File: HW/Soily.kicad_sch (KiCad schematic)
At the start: 52 parts, among them J1 USB4105-GF-A, SW1 Reset, U1 ESP32-H2-MINI-1, U2 USBLC6-2SC6, U3 AP2112K-3.3, U4 SHT30-DIS, U5 625L3C040M00000, U6 FDC2212DNTR, Y1 ABS07-32.768KHZ-T

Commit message: Cleanup component selection
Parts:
- C1: Digikey Part Number (none) -> 490-10475-1-ND; Part Number (none) -> GRM188R61A106ME69D
- C10, C11, C2, C8: Digikey Part Number (none) -> 490-5798-1-ND
- C13: Digikey Part Number (none) -> 490-4943-1-ND
- C3, C5: Digikey Part Number (none) -> 490-1543-1-ND
- C4: Digikey Part Number (none) -> 490-1543-1-ND; Part Number (none) -> GRM188R61A105KA61D
- C9: Digikey Part Number (none) -> 490-4781-1-ND
- D1: Digikey Part Number (none) -> B0520WS-FDICT-ND; Part Number (none) -> B0520WS-7-F
- D4: value XL-5050RGBC -> 150505M173300; footprint LED_SMD:LED_RGB_5050-6 -> ul_150505M173300:LED_150505M173300_WRE; Digikey Part Number (none) -> 732-12000-1-ND; Manufacturer (none) -> Würth Elektronik
- J1: Availability In Stock -> (none); Description_1 USB-C (USB TYPE-C) USB 2.0 Receptacle Connector 24 (16+8 Du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 -> (none); Digikey Part Number (none) -> 2073-USB4105-GF-ACT-ND; MP USB4110GFA -> (none); Package None -> (none); Part Number (none) -> USB4105-GF-A; Price None -> (none)
- L1: footprint Inductor_SMD:L_0603_1608Metric -> Inductor_SMD:L_1210_3225Metric; Digikey Part Number (none) -> CMH322522-180KLCT-ND
- SW1: Digikey Part Number (none) -> 4809-SKRKAHE020CT-ND; Manufacturer (none) -> Alps Alpine; Part Number (none) -> SKRKAHE020
- U1: Digikey Part Number (none) -> 1965-ESP32-H2-MINI-1-H4CT-ND
- U2: Digikey Part Number (none) -> 497-5235-1-ND; Manufacturer (none) -> STMicroelectronics; Part Number (none) -> USBLC6-2SC6
- U3: Digikey Part Number (none) -> AP2112K-3.3TRG1DICT-ND; Manufacturer (none) -> Diodes Incorporated; Part Number (none) -> AP2112K-3.3TRG1
- U4: value SHT30-DIS -> SHT40; footprint Sensor_Humidity:Sensirion_DFN-8-1EP_2.5x2.5mm_P0.5mm_EP1.1x1.7mm -> Sensor_Humidity:Sensirion_DFN-4_1.5x1.5mm_P0.8mm_SHT4x_NoCentralPad; symbol Sensor_Humidity:SHT30-DIS -> Sensor_Humidity:SHT4x; Digikey Part Number (none) -> 1649-SHT40-AD1F-R2CT-ND; Manufacturer (none) -> Sensirion AG
- U5: Digikey Part Number (none) -> 110-625L3C040M00000CT-ND; Manufacturer (none) -> CTS-Frequency Controls
- U6: value FDC2212DNTR -> FDC2212; Digikey Part Number (none) -> 296-42304-1-ND; Part Number (none) -> FDC2212DNTT
- Y1: Digikey Part Number (none) -> 535-9542-1-ND; Part Number (none) -> ABS07-32.768KHZ-T
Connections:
- net +3.3V: now also U4.3 (VDD); no longer U4.5 (VDD)
- net GND: now also U4.4 (VSS); no longer U4.2 (ADDR), U4.7 (R), U4.8 (VSS), U4.9 (VSS)
- net SCL: now also U4.2 (SCL); no longer U4.4 (SCL)
- no-connect marks 6 -> 4
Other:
- note added: "Capacitance-to-Digital"
- note added: "L-C Tank Sensor"
- note removed: "Capacitive Sense"
- moved on the sheet: C10

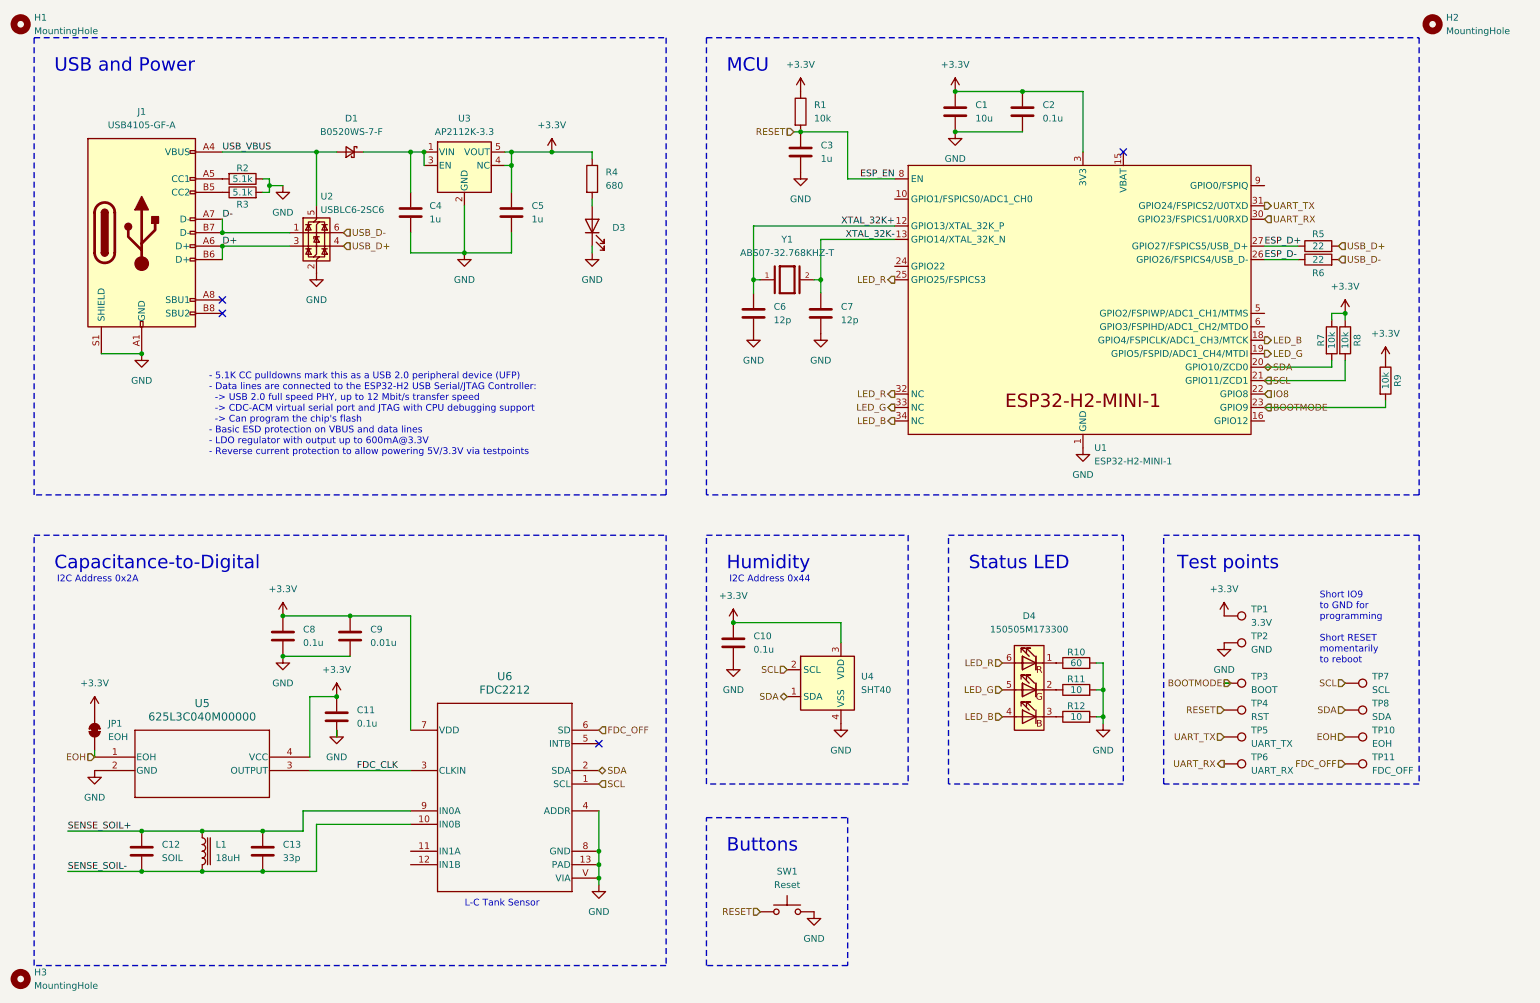
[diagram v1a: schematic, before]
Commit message: FDC2212 Breakout board
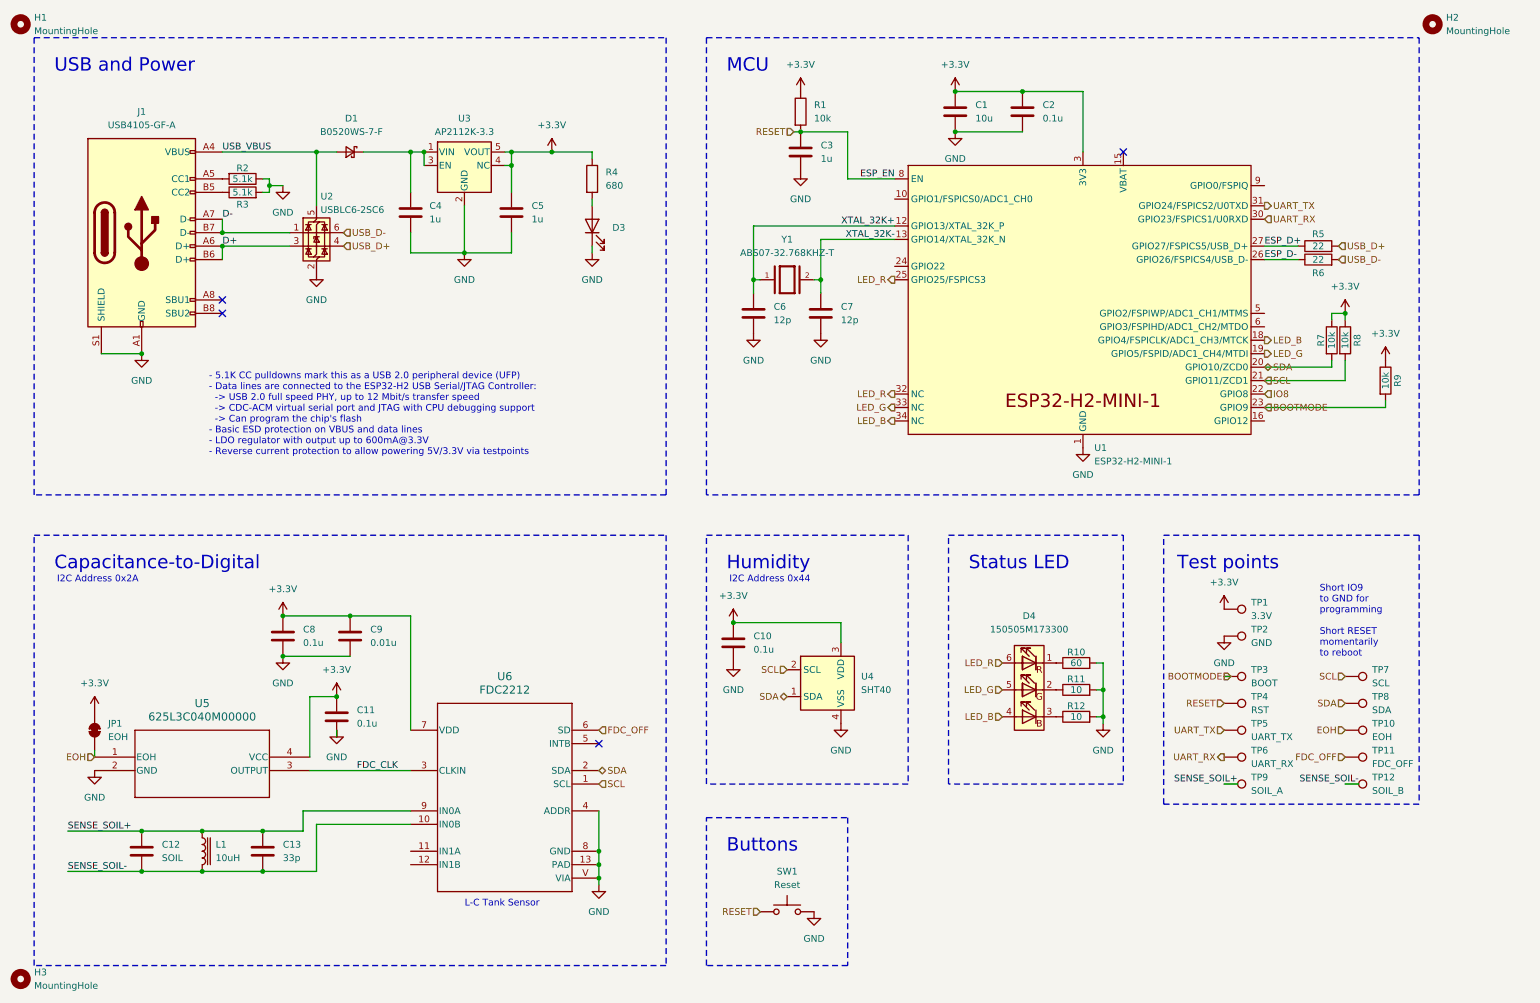
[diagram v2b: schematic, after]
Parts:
- added TP12: SOIL_B, TestPoint:TestPoint_Pad_D1.0mm, symbol Connector:TestPoint
- added TP9: SOIL_A, TestPoint:TestPoint_Pad_D1.0mm, symbol Connector:TestPoint
- C13: Digikey Part Number 490-4943-1-ND -> 490-16409-1-ND
- C6, C7: Digikey Part Number (none) -> 490-8009-1-ND
- L1: value 18uH -> 10uH; Digikey Part Number CMH322522-180KLCT-ND -> 118-CMH322522-100KLCT-ND
- R1, R7, R8, R9: Digikey Part Number (none) -> 311-10.0KHRCT-ND
- R2, R3: Digikey Part Number (none) -> 311-5.10KHRCT-ND
- R5, R6: Digikey Part Number (none) -> 311-22.0HRCT-ND
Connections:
- net SENSE_SOIL+: now also TP9.1
- net SENSE_SOIL-: now also TP12.1
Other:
- moved on the sheet: TP1, TP10, TP11, TP2, TP3, TP4, TP5, TP6, TP7, TP8
